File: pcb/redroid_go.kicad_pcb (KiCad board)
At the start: 2 copper layers, 70 x 95 mm, 100 parts, among them J1 USB4105-GF-A, J2 5051101892, J3 Conn_01x02_Pin, J4 Conn_01x10_Pin, Q1 UMH3N, Q2 PMOS, Q3 UMH3N, SW1 UP, SW10 A, SW11 SW_SPDT, SW2 DOWN, SW3 LEFT, SW4 RIGHT, SW5 MENU, SW6 VOLUME, SW7 SELECT, SW8 START, SW9 B, U1 ESP32-WROVER-E-N16R8, U2 CH340C, U3 MP2161GJ-Z, U4 XC6802A42XMR-G, U5 XC6206PxxxMR, U7 NC7SZ125M5X, U8 NC7SZ125M5X, U9 NC7SZ125M5X

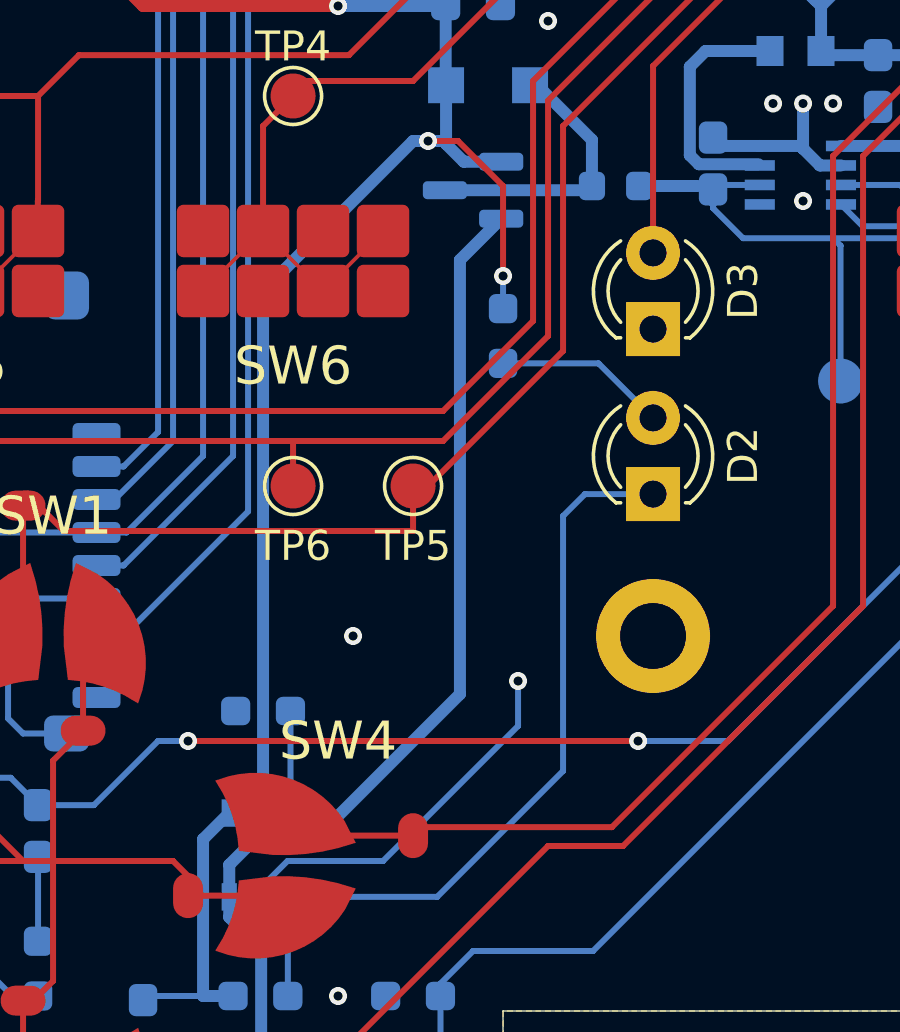
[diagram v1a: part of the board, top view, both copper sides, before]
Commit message: Fix Q2 polarity
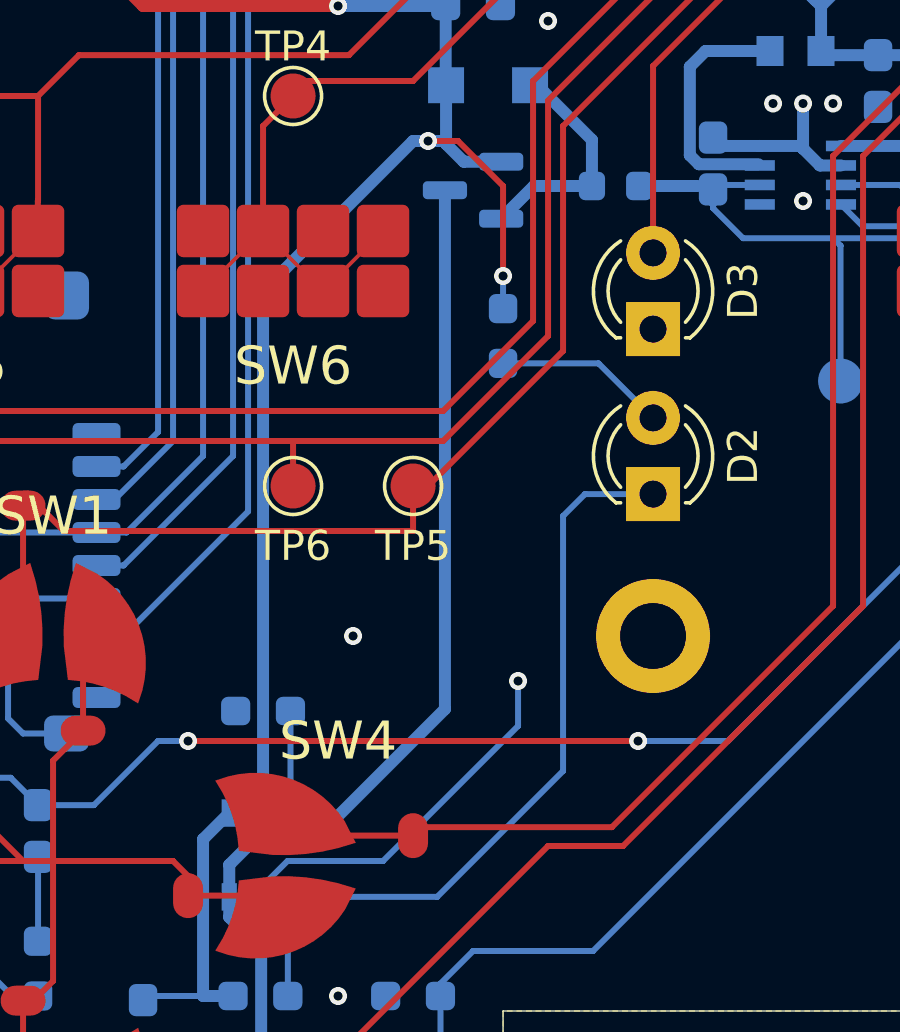
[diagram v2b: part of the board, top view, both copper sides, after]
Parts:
- PAM8304: value ~ -> PAM8304
- U6: value ~ -> uSD
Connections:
- Q2 pad 1: Net-(D1-K) -> VBAT
- Q2 pad 3: VBAT -> Net-(D1-K)
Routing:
- net Net-(D1-K): track 8.47 -> 7.51 mm
